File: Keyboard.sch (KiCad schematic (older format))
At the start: 130 parts

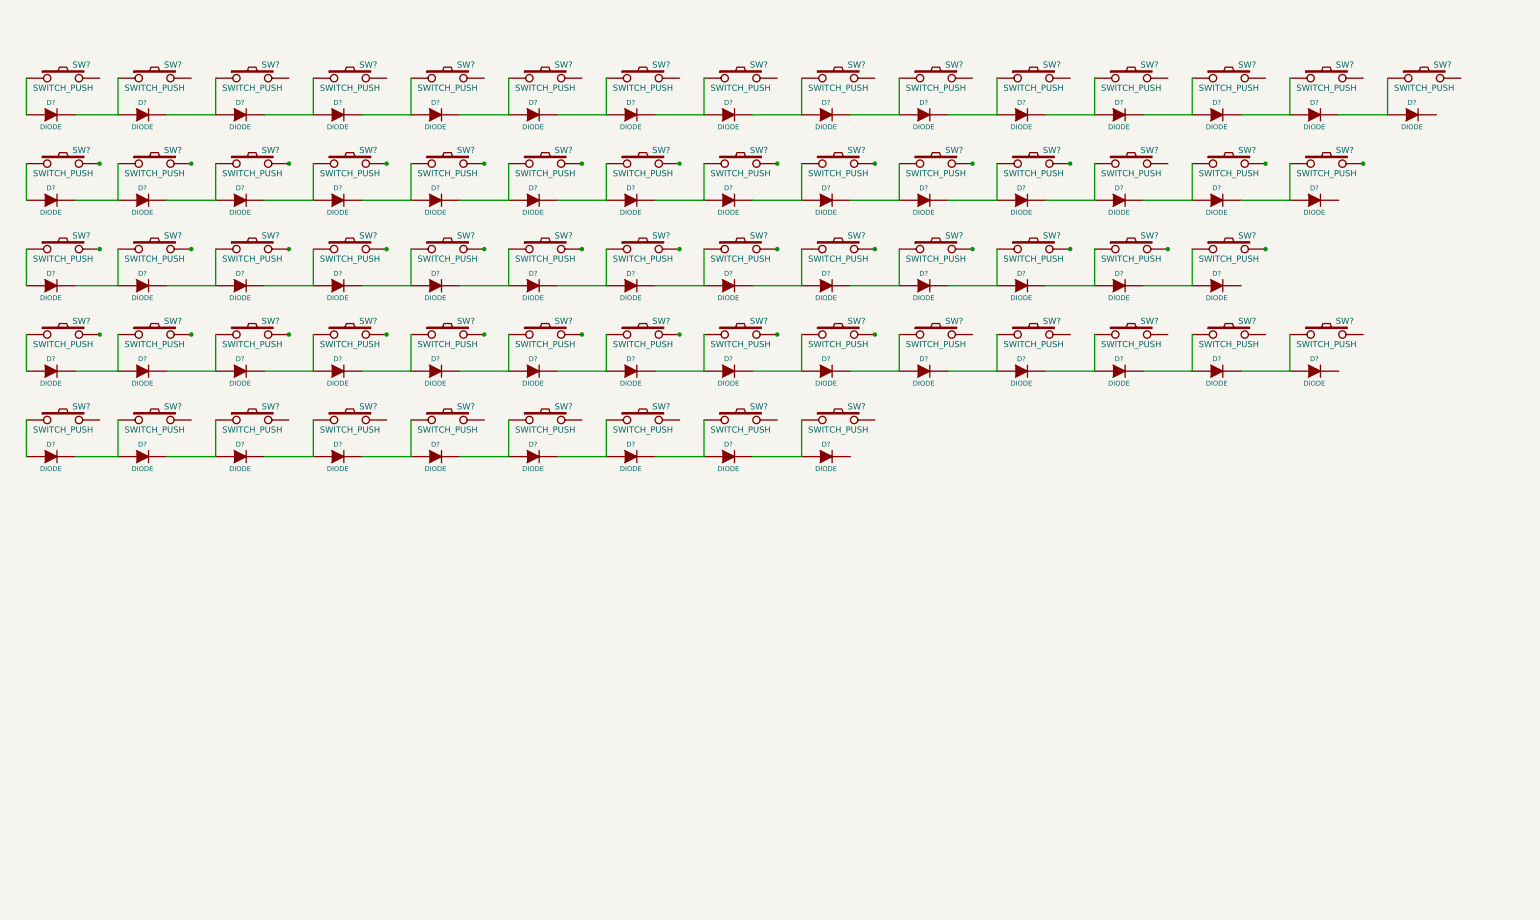
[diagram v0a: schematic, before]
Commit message: Changes to Schematic and PCB. Addition of a plate file.
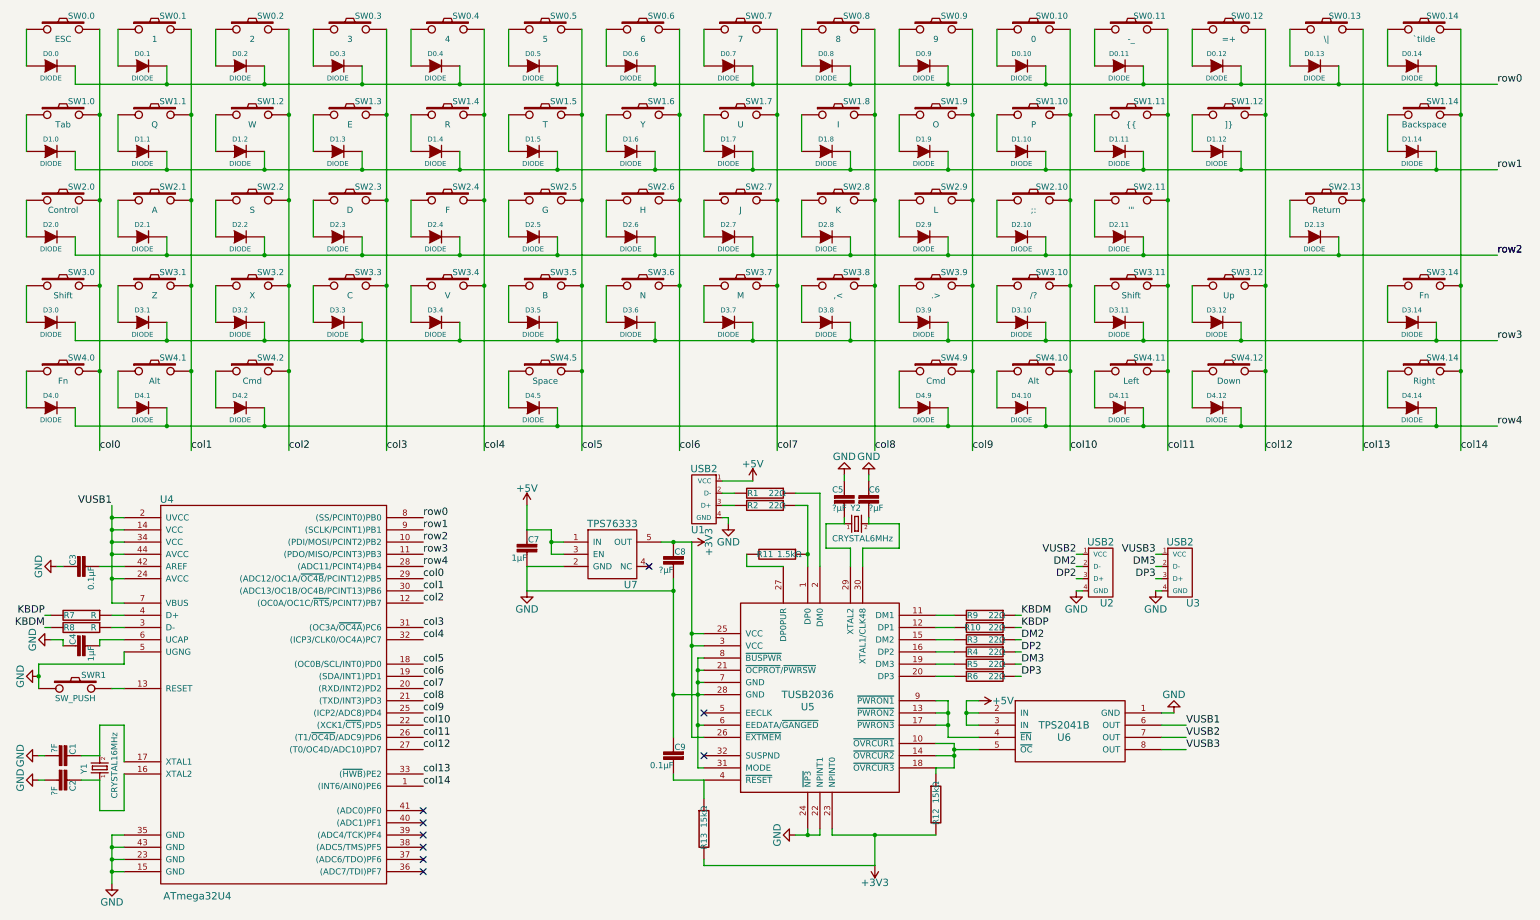
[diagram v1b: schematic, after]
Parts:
- added C1, C2: ?F, symbol CAP0805
- added C3, C9: 0.1µF, symbol CAP0805
- added C4, C7: 1µF, symbol CAP0805
- added C5, C6, C8: ?µF, symbol CAP0805
- added R1, R2, R4, R5, R6: 22Ω, symbol RESISTOR
- added R10, R3, R9: 22Ω, symbol R
- added R11: 1.5kΩ, symbol RESISTOR
- added R12, R13: 15kΩ, symbol RESISTOR
- added R7, R8: R, symbol R
- added SWR1: SW_PUSH, symbol SW_PUSH
- added U1, U2, U3: USB2, symbol USB2
- added U4: ATmega32U4, symbol ATmega32U4
- added U5: TUSB2036, symbol TUSB2036
- added U6: TPS2041B, symbol TPS2041B
- added U7: TPS76333, symbol TPS76333
- added Y1: CRYSTAL16MHz, symbol CRYSTALSMD
- added Y2: CRYSTAL6MHz, symbol CRYSTALSMD
- SW0.0: renamed from SW?; value SWITCH_PUSH -> ESC
- SW0.1: renamed from SW?; value SWITCH_PUSH -> 1
- SW0.10: renamed from SW?; value SWITCH_PUSH -> 0
- SW0.11: renamed from SW?; value SWITCH_PUSH -> -_
- SW0.12: renamed from SW?; value SWITCH_PUSH -> =+
- SW0.13: renamed from SW?; value SWITCH_PUSH -> \\|
- SW0.14: renamed from SW?; value SWITCH_PUSH -> `tilde
- SW0.2: renamed from SW?; value SWITCH_PUSH -> 2
- SW0.3: renamed from SW?; value SWITCH_PUSH -> 3
- SW0.4: renamed from SW?; value SWITCH_PUSH -> 4
- SW0.5: renamed from SW?; value SWITCH_PUSH -> 5
- SW0.6: renamed from SW?; value SWITCH_PUSH -> 6
- SW0.7: renamed from SW?; value SWITCH_PUSH -> 7
- SW0.8: renamed from SW?; value SWITCH_PUSH -> 8
- SW0.9: renamed from SW?; value SWITCH_PUSH -> 9
- SW1.0: renamed from SW?; value SWITCH_PUSH -> Tab
- SW1.1: renamed from SW?; value SWITCH_PUSH -> Q
- SW1.10: renamed from SW?; value SWITCH_PUSH -> P
- SW1.11: renamed from SW?; value SWITCH_PUSH -> {{
- SW1.12: renamed from SW?; value SWITCH_PUSH -> ]}
- SW1.14: renamed from SW?; value SWITCH_PUSH -> Backspace
- SW1.2: renamed from SW?; value SWITCH_PUSH -> W
- SW1.3: renamed from SW?; value SWITCH_PUSH -> E
- SW1.4: renamed from SW?; value SWITCH_PUSH -> R
- SW1.5: renamed from SW?; value SWITCH_PUSH -> T
- SW1.6: renamed from SW?; value SWITCH_PUSH -> Y
- SW1.7: renamed from SW?; value SWITCH_PUSH -> U
- SW1.8: renamed from SW?; value SWITCH_PUSH -> I
- SW1.9: renamed from SW?; value SWITCH_PUSH -> O
- SW2.0: renamed from SW?; value SWITCH_PUSH -> Control
- SW2.1: renamed from SW?; value SWITCH_PUSH -> A
- SW2.10: renamed from SW?; value SWITCH_PUSH -> ;:
- SW2.11: renamed from SW?; value SWITCH_PUSH -> '\"
- SW2.13: renamed from SW?; value SWITCH_PUSH -> Return
- SW2.2: renamed from SW?; value SWITCH_PUSH -> S
- SW2.3: renamed from SW?; value SWITCH_PUSH -> D
- SW2.4: renamed from SW?; value SWITCH_PUSH -> F
- SW2.5: renamed from SW?; value SWITCH_PUSH -> G
- SW2.6: renamed from SW?; value SWITCH_PUSH -> H
- SW2.7: renamed from SW?; value SWITCH_PUSH -> J
- SW2.8: renamed from SW?; value SWITCH_PUSH -> K
- SW2.9: renamed from SW?; value SWITCH_PUSH -> L
- SW3.0, SW3.11: renamed from SW?; value SWITCH_PUSH -> Shift
- SW3.1: renamed from SW?; value SWITCH_PUSH -> Z
- SW3.10: renamed from SW?; value SWITCH_PUSH -> /?
- SW3.12: renamed from SW?; value SWITCH_PUSH -> Up
- SW3.14, SW4.0: renamed from SW?; value SWITCH_PUSH -> Fn
- SW3.2: renamed from SW?; value SWITCH_PUSH -> X
- SW3.3: renamed from SW?; value SWITCH_PUSH -> C
- SW3.4: renamed from SW?; value SWITCH_PUSH -> V
- SW3.5: renamed from SW?; value SWITCH_PUSH -> B
- SW3.6: renamed from SW?; value SWITCH_PUSH -> N
- SW3.7: renamed from SW?; value SWITCH_PUSH -> M
- SW3.8: renamed from SW?; value SWITCH_PUSH -> ,<
- SW3.9: renamed from SW?; value SWITCH_PUSH -> .>
- SW4.1, SW4.10: renamed from SW?; value SWITCH_PUSH -> Alt
- SW4.11: renamed from SW?; value SWITCH_PUSH -> Left
- SW4.12: renamed from SW?; value SWITCH_PUSH -> Down
- SW4.14: renamed from SW?; value SWITCH_PUSH -> Right
- SW4.2, SW4.9: renamed from SW?; value SWITCH_PUSH -> Cmd
- SW4.5: renamed from SW?; value SWITCH_PUSH -> Space
- gave numbers to parts that had none: 65
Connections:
- net col0: now reaches SW0.0.2
- net col0: now also SW1.0.2, SW2.0.2, SW3.0.2, SW4.0.2, U4.29 ((ADC12/OC1A/~OC4B~/PCINT12)PB5)
- net at D0.1.1 (A), SW0.1.1: no longer D0.0.2 (K)
- net col1: now reaches SW0.1.2
- net col1: now also SW1.1.2, SW2.1.2, SW3.1.2, SW4.1.2, U4.30 ((ADC13/OC1B/OC4B/PCINT13)PB6)
- net at D0.2.1 (A), SW0.2.1: no longer D0.1.2 (K)
- net col2: now reaches SW0.2.2
- net col2: now also SW1.2.2, SW2.2.2, SW3.2.2, SW4.2.2, U4.12 ((OC0A/OC1C/~RTS~/PCINT7)PB7)
- net at D0.3.1 (A), SW0.3.1: no longer D0.2.2 (K)
- net col3: now reaches SW0.3.2
- net col3: now also SW1.3.2, SW2.3.2, SW3.3.2, U4.31 ((OC3A/~OC4A~)PC6)
- net at D0.4.1 (A), SW0.4.1: no longer D0.3.2 (K)
- net col4: now reaches SW0.4.2
- net col4: now also SW1.4.2, SW2.4.2, SW3.4.2, U4.32 ((ICP3/CLK0/OC4A)PC7)
- net at D0.5.1 (A), SW0.5.1: no longer D0.4.2 (K)
- net col5: now reaches SW0.5.2
- net col5: now also SW1.5.2, SW2.5.2, SW3.5.2, SW4.5.2, U4.18 ((OC0B/SCL/INT0)PD0)
- net at D0.6.1 (A), SW0.6.1: no longer D0.5.2 (K)
- net col6: now reaches SW0.6.2
- net col6: now also SW1.6.2, SW2.6.2, SW3.6.2, U4.19 ((SDA/INT1)PD1)
- net at D0.7.1 (A), SW0.7.1: no longer D0.6.2 (K)
- net col7: now reaches SW0.7.2
- net col7: now also SW1.7.2, SW2.7.2, SW3.7.2, U4.20 ((RXD/INT2)PD2)
- net at D0.8.1 (A), SW0.8.1: no longer D0.7.2 (K)
- net col8: now reaches SW0.8.2
- net col8: now also SW1.8.2, SW2.8.2, SW3.8.2, U4.21 ((TXD/INT3)PD3)
- net at D0.9.1 (A), SW0.9.1: no longer D0.8.2 (K)
- net col9: now reaches SW0.9.2
- net col9: now also SW1.9.2, SW2.9.2, SW3.9.2, SW4.9.2, U4.25 ((ICP2/ADC8)PD4)
- net at D0.10.1 (A), SW0.10.1: no longer D0.9.2 (K)
- net col10: now reaches SW0.10.2
- net col10: now also SW1.10.2, SW2.10.2, SW3.10.2, SW4.10.2, U4.22 ((XCK1/~CTS~)PD5)
- net at D0.11.1 (A), SW0.11.1: no longer D0.10.2 (K)
- net col11: now reaches SW0.11.2
- net col11: now also SW1.11.2, SW2.11.2, SW3.11.2, SW4.11.2, U4.26 ((T1/~OC4D~/ADC9)PD6)
- net at D0.12.1 (A), SW0.12.1: no longer D0.11.2 (K)
- net col12: now reaches SW0.12.2
- net col12: now also SW1.12.2, SW3.12.2, SW4.12.2, U4.27 ((T0/OC4D/ADC10)PD7)
- net at D0.13.1 (A), SW0.13.1: no longer D0.12.2 (K)
- net col13: now reaches SW0.13.2
- net col13: now also SW2.13.2, U4.33 ((~HWB~)PE2)
- net at D0.14.1 (A), SW0.14.1: no longer D0.13.2 (K)
- net col14: now reaches SW0.14.2
- net col14: now also SW1.14.2, SW3.14.2, SW4.14.2, U4.1 ((INT6/AIN0)PE6)
- net at D1.1.1 (A), SW1.1.1: no longer D1.0.2 (K)
- net at D1.2.1 (A), SW1.2.1: no longer D1.1.2 (K)
- net at D1.3.1 (A), SW1.3.1: no longer D1.2.2 (K)
- net at D1.4.1 (A), SW1.4.1: no longer D1.3.2 (K)
- net at D1.5.1 (A), SW1.5.1: no longer D1.4.2 (K)
- net at D1.6.1 (A), SW1.6.1: no longer D1.5.2 (K)
- net at D1.7.1 (A), SW1.7.1: no longer D1.6.2 (K)
- net at D1.8.1 (A), SW1.8.1: no longer D1.7.2 (K)
- net at D1.9.1 (A), SW1.9.1: no longer D1.8.2 (K)
- net at D1.10.1 (A), SW1.10.1: no longer D1.9.2 (K)
- net at D1.11.1 (A), SW1.11.1: no longer D1.10.2 (K)
- net at D1.12.1 (A), SW1.12.1: no longer D1.11.2 (K)
- net at D1.14.1 (A), SW1.14.1: no longer D1.12.2 (K)
- net at D2.1.1 (A), SW2.1.1: no longer D2.0.2 (K)
- net at D2.2.1 (A), SW2.2.1: no longer D2.1.2 (K)
- net at D2.3.1 (A), SW2.3.1: no longer D2.2.2 (K)
- net at D2.4.1 (A), SW2.4.1: no longer D2.3.2 (K)
- net at D2.5.1 (A), SW2.5.1: no longer D2.4.2 (K)
- net at D2.6.1 (A), SW2.6.1: no longer D2.5.2 (K)
- net at D2.7.1 (A), SW2.7.1: no longer D2.6.2 (K)
- net at D2.8.1 (A), SW2.8.1: no longer D2.7.2 (K)
- net at D2.9.1 (A), SW2.9.1: no longer D2.8.2 (K)
- net at D2.10.1 (A), SW2.10.1: no longer D2.9.2 (K)
- net at D2.11.1 (A), SW2.11.1: no longer D2.10.2 (K)
- net at D2.13.1 (A), SW2.13.1: no longer D2.11.2 (K)
- net at D3.1.1 (A), SW3.1.1: no longer D3.0.2 (K)
- net at D3.2.1 (A), SW3.2.1: no longer D3.1.2 (K)
- net at D3.3.1 (A), SW3.3.1: no longer D3.2.2 (K)
- net at D3.4.1 (A), SW3.4.1: no longer D3.3.2 (K)
- net at D3.5.1 (A), SW3.5.1: no longer D3.4.2 (K)
- net at D3.6.1 (A), SW3.6.1: no longer D3.5.2 (K)
- net at D3.7.1 (A), SW3.7.1: no longer D3.6.2 (K)
- net at D3.8.1 (A), SW3.8.1: no longer D3.7.2 (K)
- net at D3.9.1 (A), SW3.9.1: no longer D3.8.2 (K)
- net at D3.10.1 (A), SW3.10.1: no longer D3.9.2 (K)
- net at D3.11.1 (A), SW3.11.1: no longer D3.10.2 (K)
- net at D3.12.1 (A), SW3.12.1: no longer D3.11.2 (K)
- net at D3.14.1 (A), SW3.14.1: no longer D3.12.2 (K)
- net at D4.1.1 (A), SW4.1.1: no longer D4.0.2 (K)
- net at D4.2.1 (A), SW4.2.1: no longer D4.1.2 (K)
- net at D4.5.1 (A), SW4.5.1: no longer D4.2.2 (K)
- net at D4.9.1 (A), SW4.9.1: no longer D4.5.2 (K)
- net at D4.10.1 (A), SW4.10.1: no longer D4.9.2 (K)
- net at D4.11.1 (A), SW4.11.1: no longer D4.10.2 (K)
- net at D4.12.1 (A), SW4.12.1: no longer D4.11.2 (K)
- net at D4.14.1 (A), SW4.14.1: no longer D4.12.2 (K)
- net row0: now reaches D0.14.2 (K)
- net row0: now also D0.0.2 (K), D0.1.2 (K), D0.10.2 (K), D0.11.2 (K), D0.12.2 (K), D0.13.2 (K), D0.2.2 (K), D0.3.2 (K), D0.4.2 (K), D0.5.2 (K), D0.6.2 (K), D0.7.2 (K), D0.8.2 (K), D0.9.2 (K), U4.8 ((SS/PCINT0)PB0)
- net row1: now reaches D1.14.2 (K)
- net row1: now also D1.0.2 (K), D1.1.2 (K), D1.10.2 (K), D1.11.2 (K), D1.12.2 (K), D1.2.2 (K), D1.3.2 (K), D1.4.2 (K), D1.5.2 (K), D1.6.2 (K), D1.7.2 (K), D1.8.2 (K), D1.9.2 (K), U4.9 ((SCLK/PCINT1)PB1)
- net row2: now reaches D2.13.2 (K)
- net row2: now also D2.0.2 (K), D2.1.2 (K), D2.10.2 (K), D2.11.2 (K), D2.2.2 (K), D2.3.2 (K), D2.4.2 (K), D2.5.2 (K), D2.6.2 (K), D2.7.2 (K), D2.8.2 (K), D2.9.2 (K), U4.10 ((PDI/MOSI/PCINT2)PB2)
- net row3: now reaches D3.14.2 (K)
- net row3: now also D3.0.2 (K), D3.1.2 (K), D3.10.2 (K), D3.11.2 (K), D3.12.2 (K), D3.2.2 (K), D3.3.2 (K), D3.4.2 (K), D3.5.2 (K), D3.6.2 (K), D3.7.2 (K), D3.8.2 (K), D3.9.2 (K), U4.11 ((PDO/MISO/PCINT3)PB3)
- net row4: now reaches D4.14.2 (K)
- net row4: now also D4.0.2 (K), D4.1.2 (K), D4.10.2 (K), D4.11.2 (K), D4.12.2 (K), D4.2.2 (K), D4.5.2 (K), D4.9.2 (K), U4.28 ((ADC11/PCINT4)PB4)
- new net: R11.1, R2.1, U5.1 (DP0)
- new net: R12.1, U5.10 (~OVRCUR1), U5.14 (~OVRCUR2), U5.18 (~OVRCUR3), U6.5 (~OC)
- new net: R9.2, U5.11 (DM1)
- new net: R10.2, U5.12 (DP1)
- new net: U5.13 (~PWRON2), U5.17 (~PWRON3), U5.9 (~PWRON1), U6.4 (~EN)
- new net: R3.2, U5.15 (DM2)
- new net: R4.2, U5.16 (DP2)
- new net: R5.2, U5.19 (DM3)
- new net: R1.1, U5.2 (DM0)
- new net: R6.2, U5.20 (DP3)
- new net: R11.2, U5.27 (DP0PUR)
- new net: C5.2, U5.29 (XTAL2), Y2.1
- new net: C6.2, U5.30 (XTAL1/CLK48), Y2.2
- new net: C9.1, R13.1, U5.4 (~RESET)
- new net: SWR1.2, U4.13 (RESET)
- new net: C2.1, U4.16 (XTAL2), Y1.1
- new net: C1.1, U4.17 (XTAL1), Y1.2
- new net: R8.1, U4.3 (D-)
- new net: R7.1, U4.4 (D+)
- new net: C3.1, U4.42 (AREF)
- new net: C4.1, U4.6 (UCAP)
- new net: R1.2, U1.2 (D-)
- new net: R2.2, U1.3 (D+)
- new net +3V3: C8.2, R12.2, R13.2, U5.23 (NPINT0), U5.25 (VCC), U5.26 (~EXTMEM), U5.3 (VCC), U7.5 (OUT)
- new net +5V: C7.2, U1.1 (VCC), U6.2 (IN), U6.3 (IN), U7.1 (IN), U7.3 (EN)
- new net DM2: R3.1, U2.2 (D-)
- new net DM3: R5.1, U3.2 (D-)
- new net DP2: R4.1, U2.3 (D+)
- new net DP3: R6.1, U3.3 (D+)
- new net GND: C1.2, C2.2, C3.2, C4.2, C5.1, C6.1, C7.1, C8.1, C9.2, SWR1.1, U1.4 (GND), U2.4 (GND), U3.4 (GND), U4.15 (GND), U4.23 (GND), U4.35 (GND), U4.43 (GND), U4.5 (UGNG), U5.21 (~OCPROT~/~PWRSW), U5.22 (NPINT1), U5.24 (~NP3), U5.28 (GND), U5.31 (MODE), U5.6 (EEDATA/~GANGED), U5.7 (GND), U5.8 (~BUSPWR), U6.1 (GND), U7.2 (GND)
- new net KBDM: R8.2, R9.1
- new net KBDP: R10.1, R7.2
- new net VUSB1: U4.14 (VCC), U4.2 (UVCC), U4.24 (AVCC), U4.34 (VCC), U4.44 (AVCC), U4.7 (VBUS), U6.6 (OUT)
- new net VUSB2: U2.1 (VCC), U6.7 (OUT)
- new net VUSB3: U3.1 (VCC), U6.8 (OUT)
- no-connect marks 0 -> 9
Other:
- moved on the sheet: D0.0, D0.1, D0.10, D0.11, D0.12, D0.13, D0.14, D0.2, D0.3, D0.4, D0.5, D0.6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
